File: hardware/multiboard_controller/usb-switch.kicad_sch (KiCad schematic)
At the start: 1 part, among them U1 max4999etj+

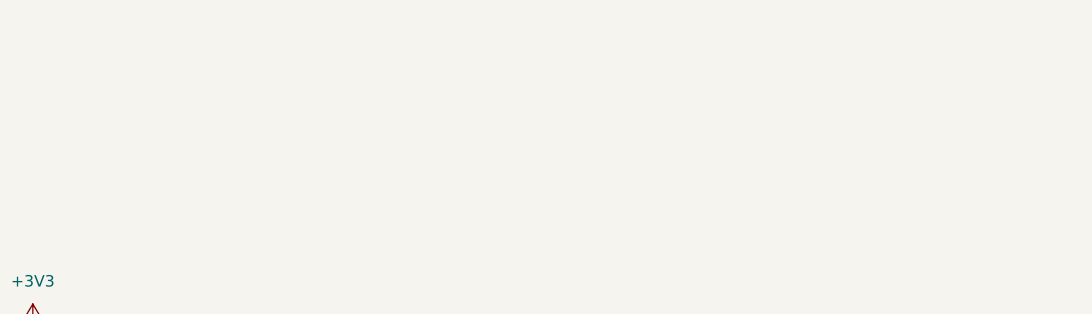
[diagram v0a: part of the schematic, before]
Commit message: Adding final connectors and general cleanup.
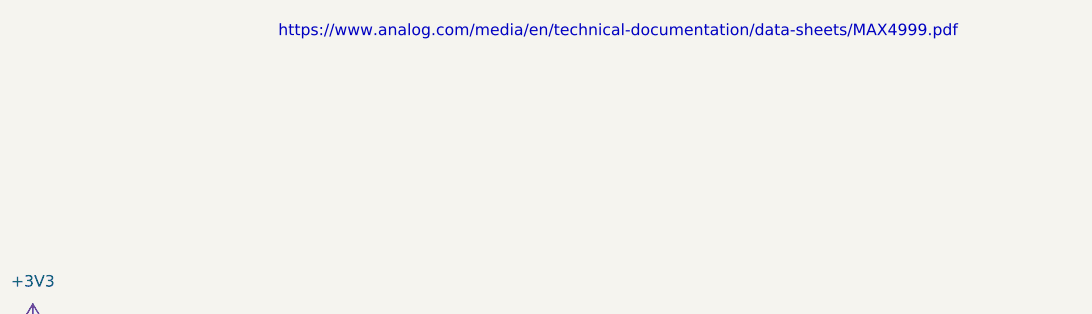
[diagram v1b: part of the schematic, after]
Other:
- note added: "https://www.analog.com/media/en/technical-documentation/data-sheets/MAX4999.pdf"
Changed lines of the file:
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@@
+		)
+	)
+	(text "https://www.analog.com/media/en/technical-documentation/data-sheets/MAX4999.pdf"
+		(exclude_from_sim no)
+		(at 232.664 20.574 0)
+		(effects
+			(font
+				(size 1.27 1.27)
+			)
 		)
 	)
@@
 			)
 		)
-		(property "Datasheet" "max4999etj+"
+		(property "Datasheet" "https://www.analog.com/media/en/technical-documentation/data-sheets/MAX4999.pdf"
 			(at 119.38 58.42 0)
 			(effects

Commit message: Starting layout
Add serial ground connections, add footprint libraries, start layout.
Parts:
- U1: footprint 21-0140_T3255+4_MXM -> all-footprints:21-0140_T3255&plus_4_MXM-M
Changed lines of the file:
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@@
 			)
 		)
-		(property "Description" ""
+		(property "Description" "Power symbol creates a global label with name \"GND\" , ground"
 			(at 115.57 106.68 0)
 			(effects
@@
 			)
 		)
-		(property "Description" ""
+		(property "Description" "Power symbol creates a global label with name \"GND\" , ground"
 			(at 165.1 106.68 0)
 			(effects
@@
 			)
 		)
-		(property "Description" ""
+		(property "Description" "Power symbol creates a global label with name \"+3V3\""
 			(at 167.64 53.34 0)
 			(effects
@@
 			)
 		)
-		(property "Footprint" "21-0140_T3255+4_MXM"
+		(property "Footprint" "all-footprints:21-0140_T3255&plus_4_MXM-M"
 			(at 119.38 58.42 0)
 			(effects
@@
 			)
 		)
-		(property "Description" ""
+		(property "Description" "Power symbol creates a global label with name \"+3V3\""
 			(at 113.03 53.34 0)
 			(effects
